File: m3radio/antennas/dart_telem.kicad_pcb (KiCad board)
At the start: 2 copper layers, 138 x 134 mm, 5 parts

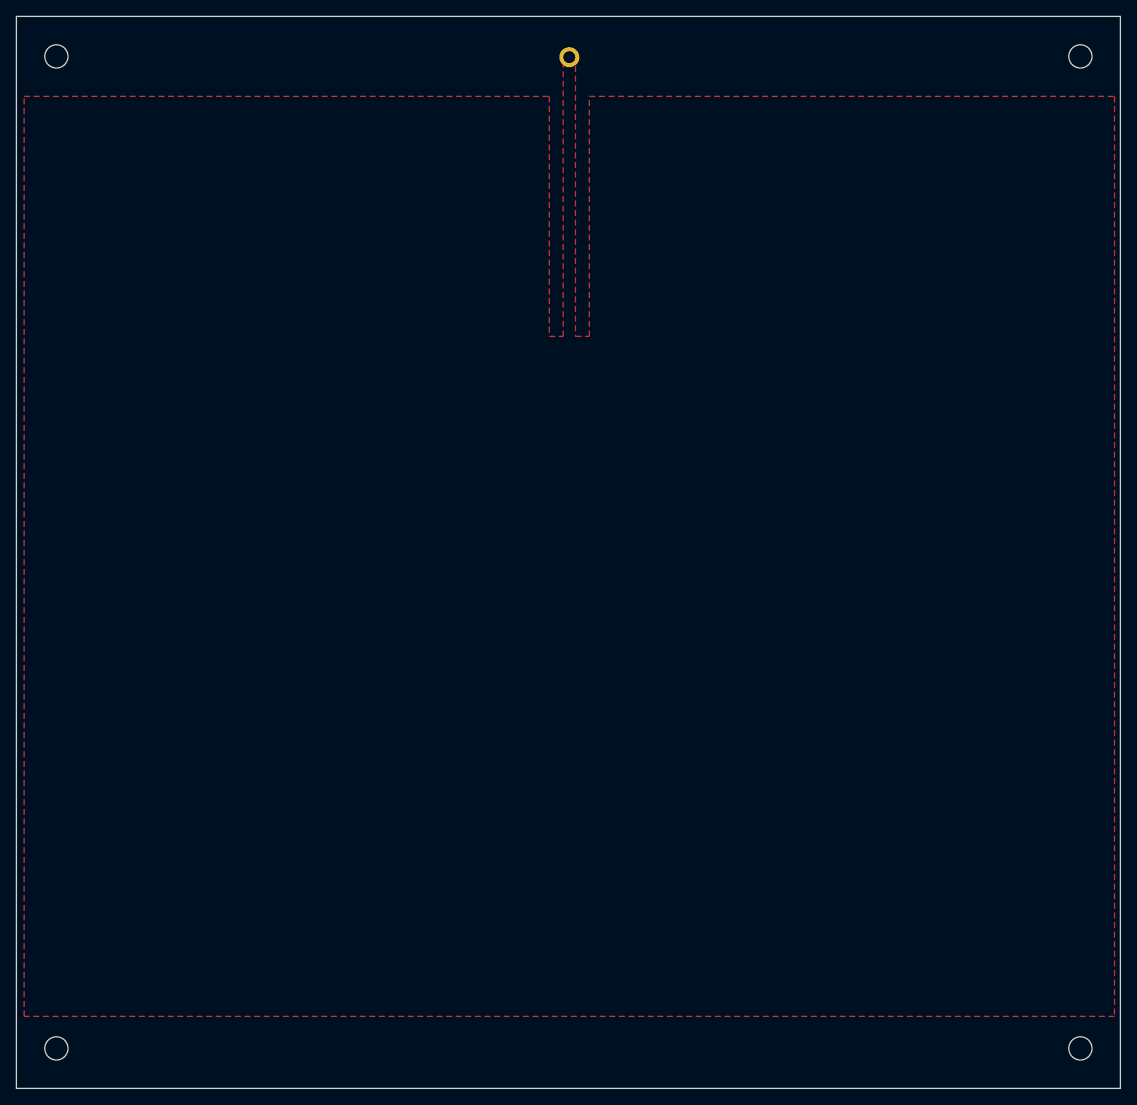
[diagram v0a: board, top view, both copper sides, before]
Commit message: make smaller dart antenna cutouts to ease manufacture
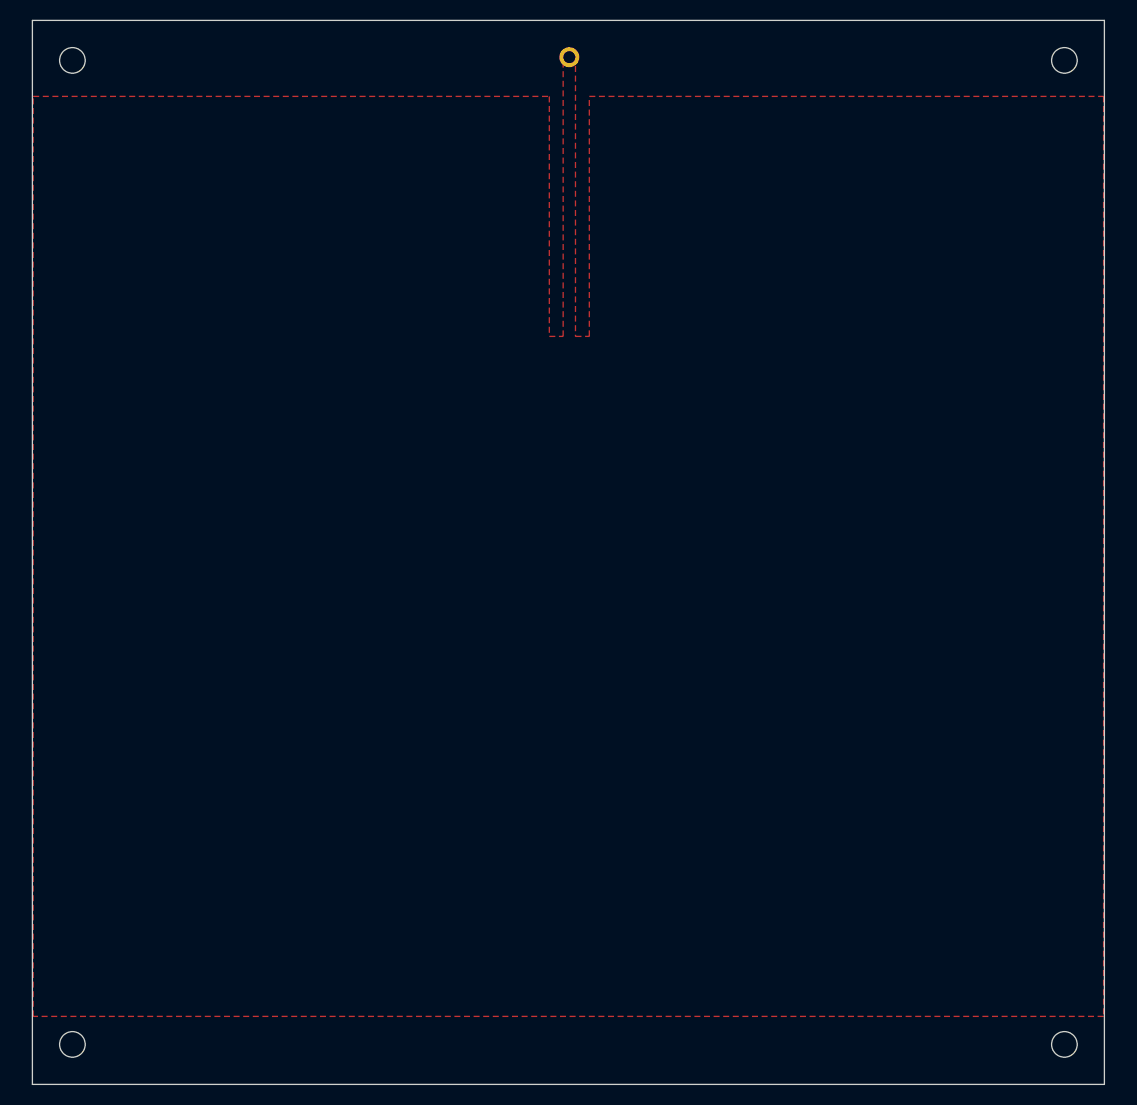
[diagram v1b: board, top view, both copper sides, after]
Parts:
- moved ? 2.06 mm to (27.0, 148.5)
- moved ? 2.06 mm to (151.0, 148.5)
- moved ? 2.06 mm to (151.0, 25.5)
- moved ? 2.06 mm to (27.0, 25.5)
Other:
- board size 138 x 134 mm -> 134 x 133 mm
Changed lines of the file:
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@@
-(kicad_pcb (version 20160815) (host pcbnew no-vcs-found-7520~57~ubuntu14.04.1)
+(kicad_pcb (version 20170123) (host pcbnew no-vcs-found-7587~57~ubuntu14.04.1)
   (general
     (links 0)
     (no_connects 0)
-    (area 19.949999 19.949999 158.050001 154.050001)
+    (area 21.949999 20.449999 156.050001 153.550001)
     (thickness 1.6)
     (drawings 4)
@@
     (mod_text_size 1 1)
     (mod_text_width 0.15)
-    (pad_size 1.524 1.524)
-    (pad_drill 0.762)
+    (pad_size 3.2 3.2)
+    (pad_drill 3.2)
     (pad_to_mask_clearance 0.2)
     (aux_axis_origin 0 0)
@@
       (psnegative false)
       (psa4output false)
-      (plotreference true)
-      (plotvalue true)
+      (plotreference false)
+      (plotvalue false)
       (plotinvisibletext false)
       (padsonsilk false)
@@
   )
   (module X0 (layer F.Cu)
-    (at 25 149)
+    (at 27 148.5)
     (fp_text reference "" (at 0 0) (layer F.SilkS)
       (effects (font (thickness 0.15)))
@@
       (effects (font (thickness 0.15)))
     )
-    (pad "" np_thru_hole circle (at 0 0) (size 2.9 2.9) (drill 2.9) (layers *.Cu *.Mask)
+    (pad "" np_thru_hole circle (at 0 0) (size 3.2 3.2) (drill 3.2) (layers *.Cu *.Mask)
       (zone_connect 2))
   )
   (module X0 (layer F.Cu)
-    (at 153 149)
+    (at 151 148.5)
     (fp_text reference "" (at 0 0) (layer F.SilkS)
       (effects (font (thickness 0.15)))
@@
       (effects (font (thickness 0.15)))
     )
-    (pad "" np_thru_hole circle (at 0 0) (size 2.9 2.9) (drill 2.9) (layers *.Cu *.Mask)
+    (pad "" np_thru_hole circle (at 0 0) (size 3.2 3.2) (drill 3.2) (layers *.Cu *.Mask)
       (zone_connect 2))
   )
   (module X0 (layer F.Cu)
-    (at 153 25)
+    (at 151 25.5)
     (fp_text reference "" (at 0 0) (layer F.SilkS)
       (effects (font (thickness 0.15)))
@@
       (effects (font (thickness 0.15)))
     )
-    (pad "" np_thru_hole circle (at 0 0) (size 2.9 2.9) (drill 2.9) (layers *.Cu *.Mask)
+    (pad "" np_thru_hole circle (at 0 0) (size 3.2 3.2) (drill 3.2) (layers *.Cu *.Mask)
       (zone_connect 2))
   )
   (module X0 (layer F.Cu)
-    (at 25 25)
+    (at 27 25.5)
     (fp_text reference "" (at 0 0) (layer F.SilkS)
       (effects (font (thickness 0.15)))
@@
       (effects (font (thickness 0.15)))
     )
-    (pad "" np_thru_hole circle (at 0 0) (size 2.9 2.9) (drill 2.9) (layers *.Cu *.Mask)
+    (pad "" np_thru_hole circle (at 0 0) (size 3.2 3.2) (drill 3.2) (layers *.Cu *.Mask)
       (zone_connect 2))
   )
@@
       (net 1 Antennas) (zone_connect 2))
   )
-  (gr_line (start 20 154) (end 20 20) (layer Edge.Cuts) (width 0.1))
-  (gr_line (start 20 20) (end 158 20) (layer Edge.Cuts) (width 0.1))
-  (gr_line (start 158 20) (end 158 154) (layer Edge.Cuts) (width 0.1))
-  (gr_line (start 158 154) (end 20 154) (layer Edge.Cuts) (width 0.1))
+  (gr_line (start 22 153.5) (end 22 20.5) (layer Edge.Cuts) (width 0.1))
+  (gr_line (start 22 20.5) (end 156 20.5) (layer Edge.Cuts) (width 0.1))
+  (gr_line (start 156 20.5) (end 156 153.5) (layer Edge.Cuts) (width 0.1))
+  (gr_line (start 156 153.5) (end 22 153.5) (layer Edge.Cuts) (width 0.1))
   (zone (net 1) (net_name Antennas) (layer F.Cu) (hatch edge 0.5)
     (connect_pads (clearance 0.3))
@@
     (polygon
       (pts
-        (xy 89.885 60) (xy 91.615 60) (xy 91.615 30) (xy 157.265 30) (xy 157.265 145)
-        (xy 20.965 145) (xy 20.965 30) (xy 86.615 30) (xy 86.615 60) (xy 88.345 60)
+        (xy 89.885 60) (xy 91.615 60) (xy 91.615 30) (xy 155.9 30) (xy 155.9 145)
+        (xy 22.1 145) (xy 22.1 30) (xy 86.615 30) (xy 86.615 60) (xy 88.345 60)
         (xy 88.345 25) (xy 89.885 25)
       )
